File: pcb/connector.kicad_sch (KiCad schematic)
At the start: 7 parts

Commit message: small updates to silkscreen and logo
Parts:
- H1, H2: footprint zzkeeb:Hole_M2 -> zzkeeb:Hole_M2-TH
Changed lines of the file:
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@@
       (effects (font (size 1.27 1.27)) (justify left))
     )
-    (property "Footprint" "zzkeeb:Hole_M2" (at 154.94 39.37 0)
+    (property "Footprint" "zzkeeb:Hole_M2-TH" (at 154.94 39.37 0)
       (effects (font (size 1.27 1.27)) hide)
     )
@@
       (effects (font (size 1.27 1.27)) (justify left))
     )
-    (property "Footprint" "zzkeeb:Hole_M2" (at 154.94 45.72 0)
+    (property "Footprint" "zzkeeb:Hole_M2-TH" (at 154.94 45.72 0)
       (effects (font (size 1.27 1.27)) hide)
     )

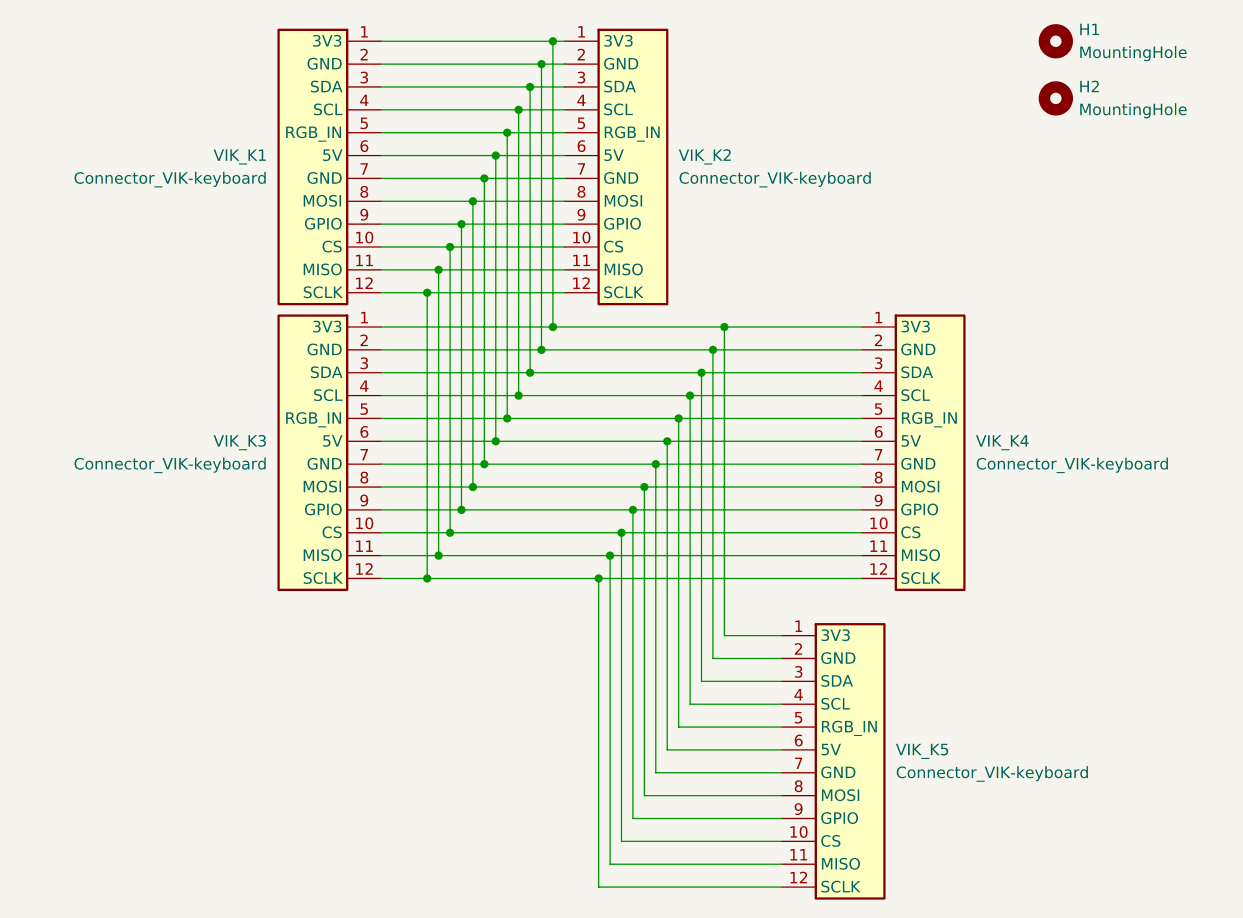
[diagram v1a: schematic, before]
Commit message: simplify connector and reduce size
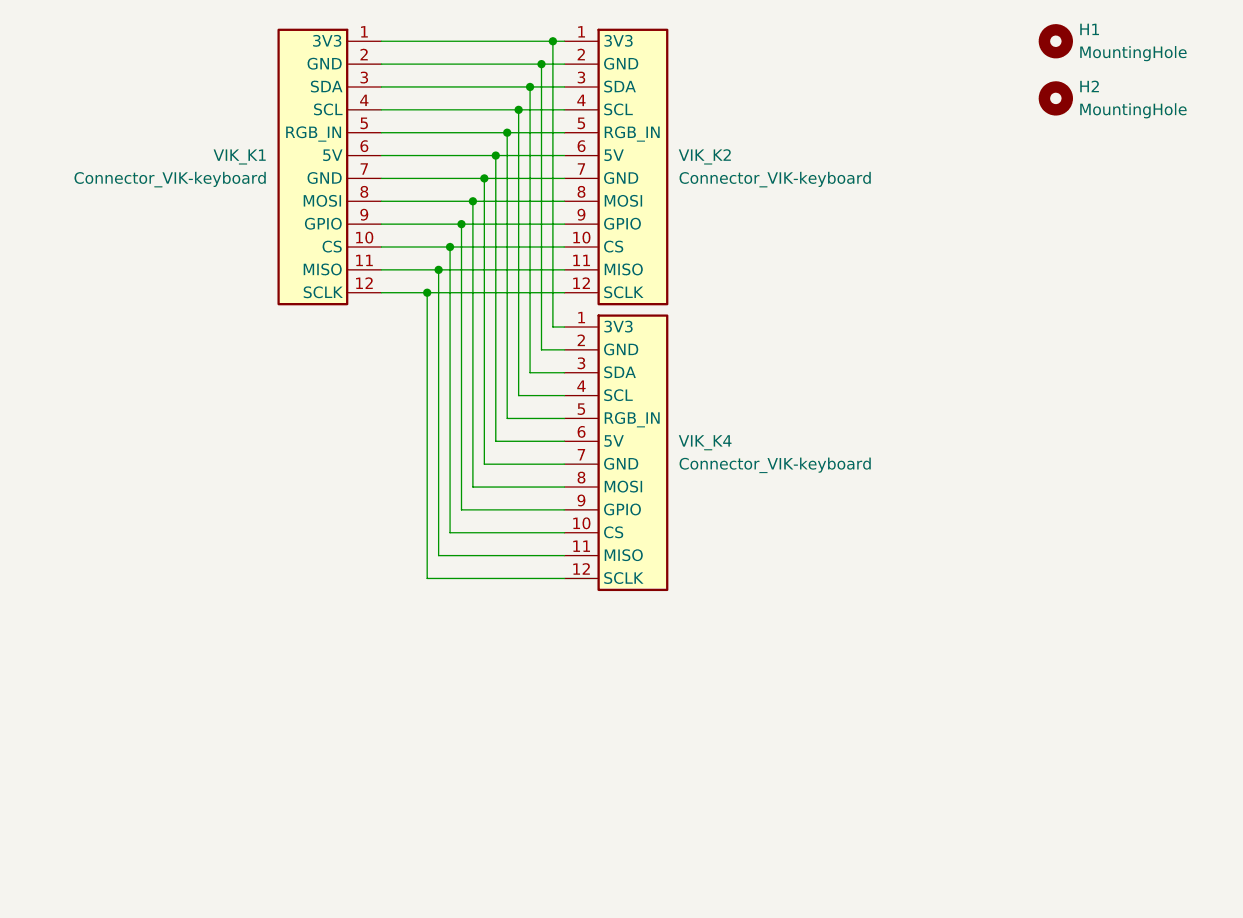
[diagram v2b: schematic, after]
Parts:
- removed VIK_K3, VIK_K5: Connector_VIK-keyboard, zzkeeb:Connector_JST-1x12-P1.25mm-vertical, symbol zzkeeb:Connector_VIK-keyboard
- VIK_K2, VIK_K4: footprint zzkeeb:Connector_VIK-vertical-keyboard -> zzkeeb:Connector_FFC-12pin-1mm-vertical
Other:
- moved on the sheet: VIK_K4
